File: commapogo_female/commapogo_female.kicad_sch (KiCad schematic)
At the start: 6 parts, among them J1 Conn_02x07_Row_Letter_Last, J2 Conn_02x12_Row_Letter_Last

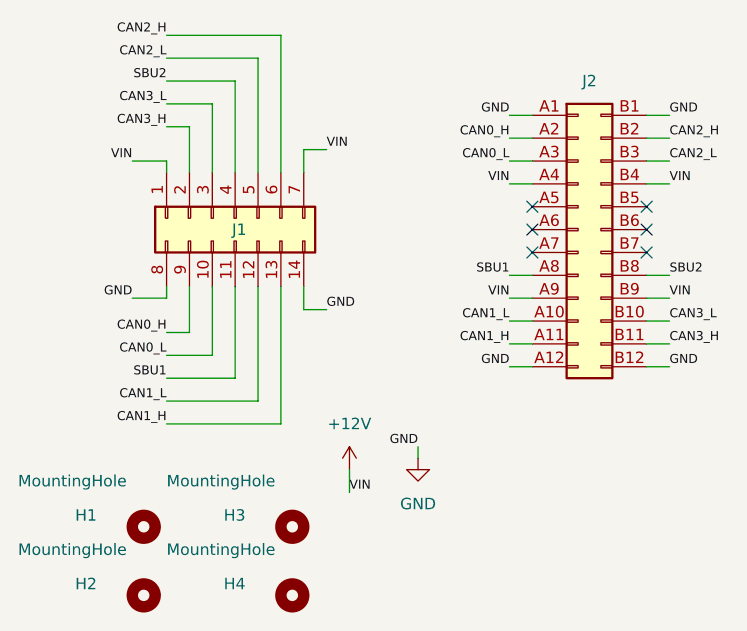
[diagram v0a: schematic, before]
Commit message: revise pcb with proper calculations
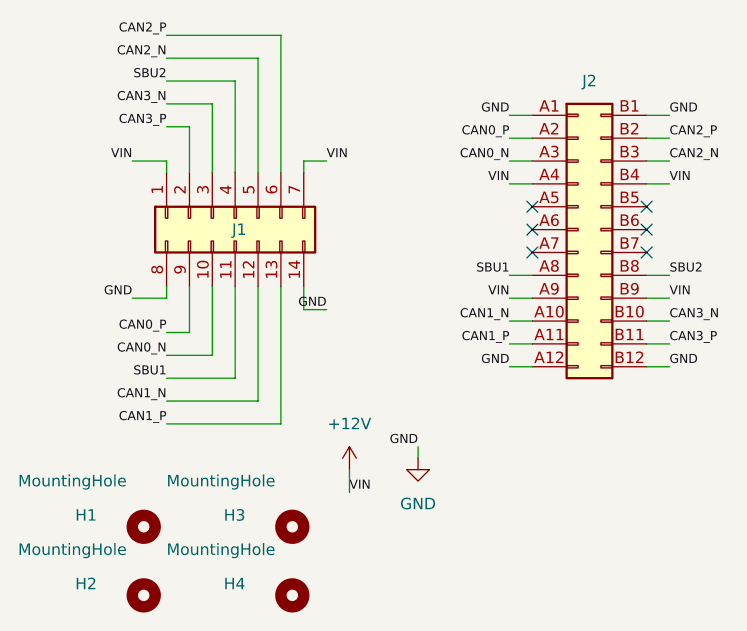
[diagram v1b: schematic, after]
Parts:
- J1: footprint CommaPogo_Library:2x7_Pogo_Female -> CommaPogo_Library:2x7_Pogo_Male
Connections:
- net CAN0_H renamed CAN0_P
- net CAN0_L renamed CAN0_N
- net CAN1_H renamed CAN1_P
- net CAN1_L renamed CAN1_N
- net CAN2_H renamed CAN2_P
- net CAN2_L renamed CAN2_N
- net CAN3_H renamed CAN3_P
- net CAN3_L renamed CAN3_N
